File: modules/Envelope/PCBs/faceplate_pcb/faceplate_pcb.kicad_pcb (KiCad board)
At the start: 2 copper layers, 40.3 x 128.5 mm, 0 parts

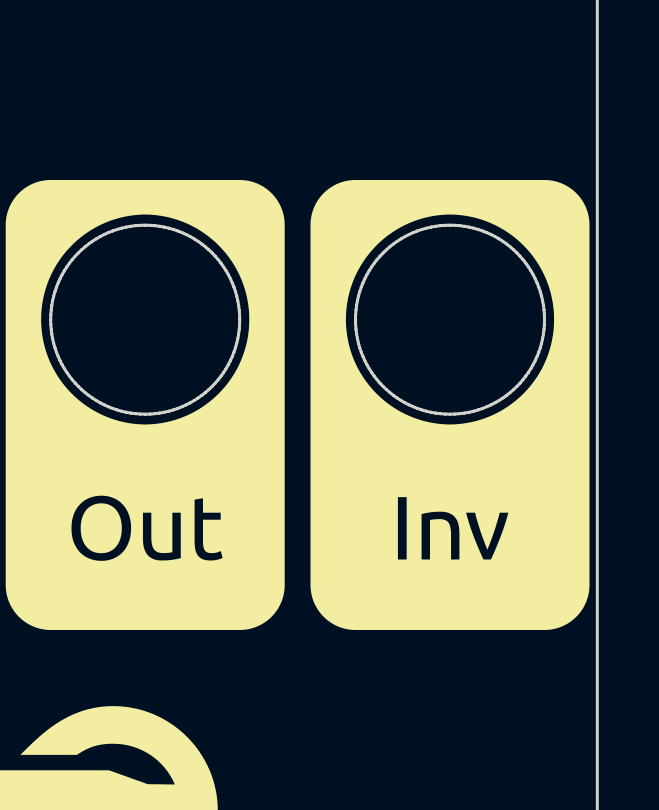
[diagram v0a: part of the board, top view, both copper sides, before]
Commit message: update envelope faceplate text
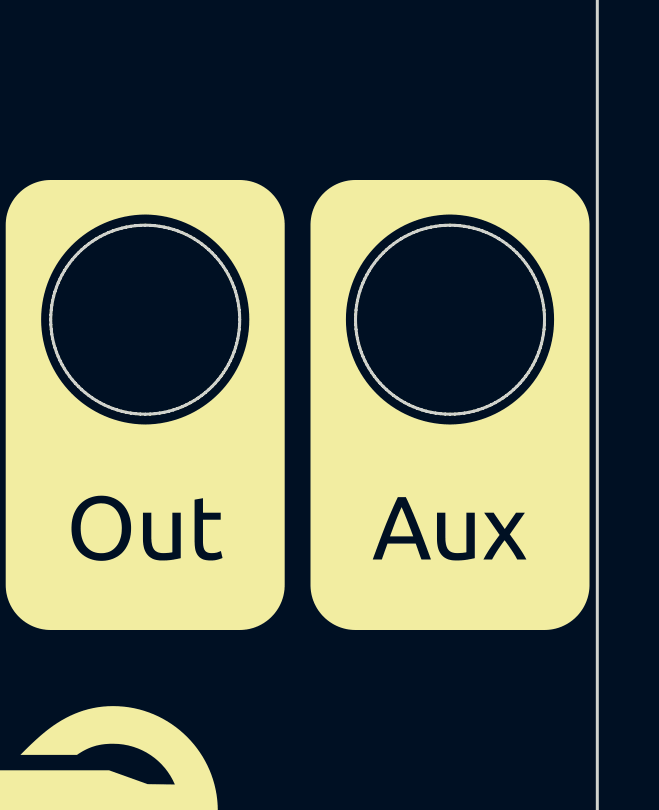
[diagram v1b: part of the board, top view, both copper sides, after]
